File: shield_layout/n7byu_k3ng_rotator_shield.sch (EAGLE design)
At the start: 23 parts, among them J1 ARDUINO_R3_SHIELD

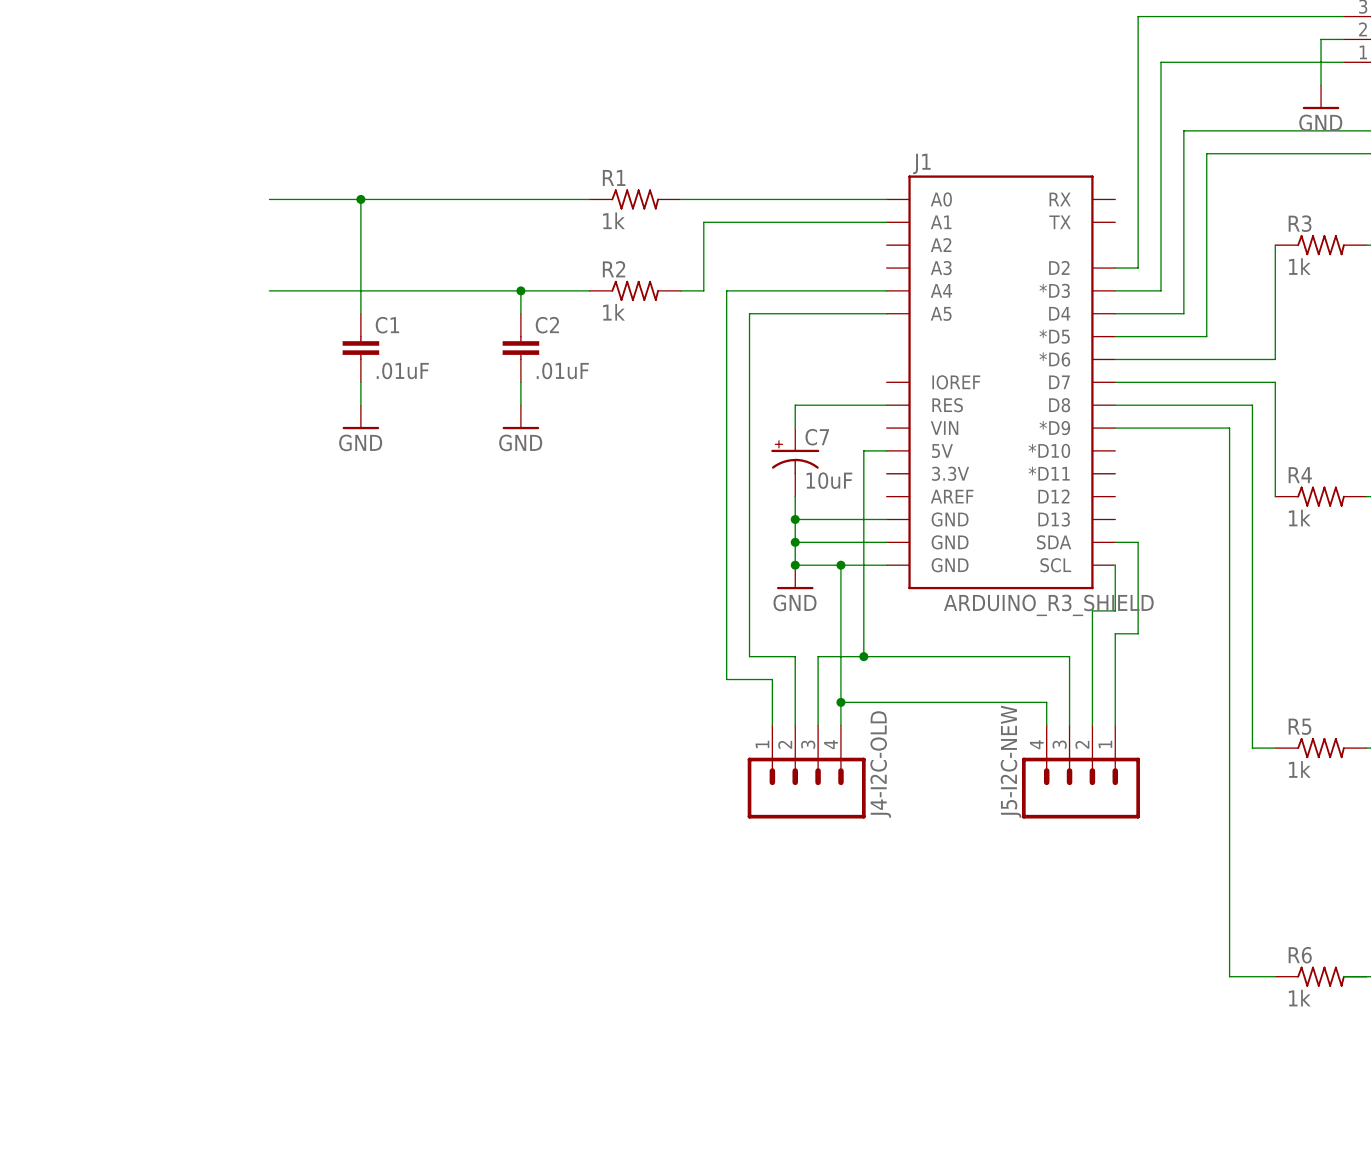
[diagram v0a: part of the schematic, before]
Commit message: jumpers for park, stop, reset buttons
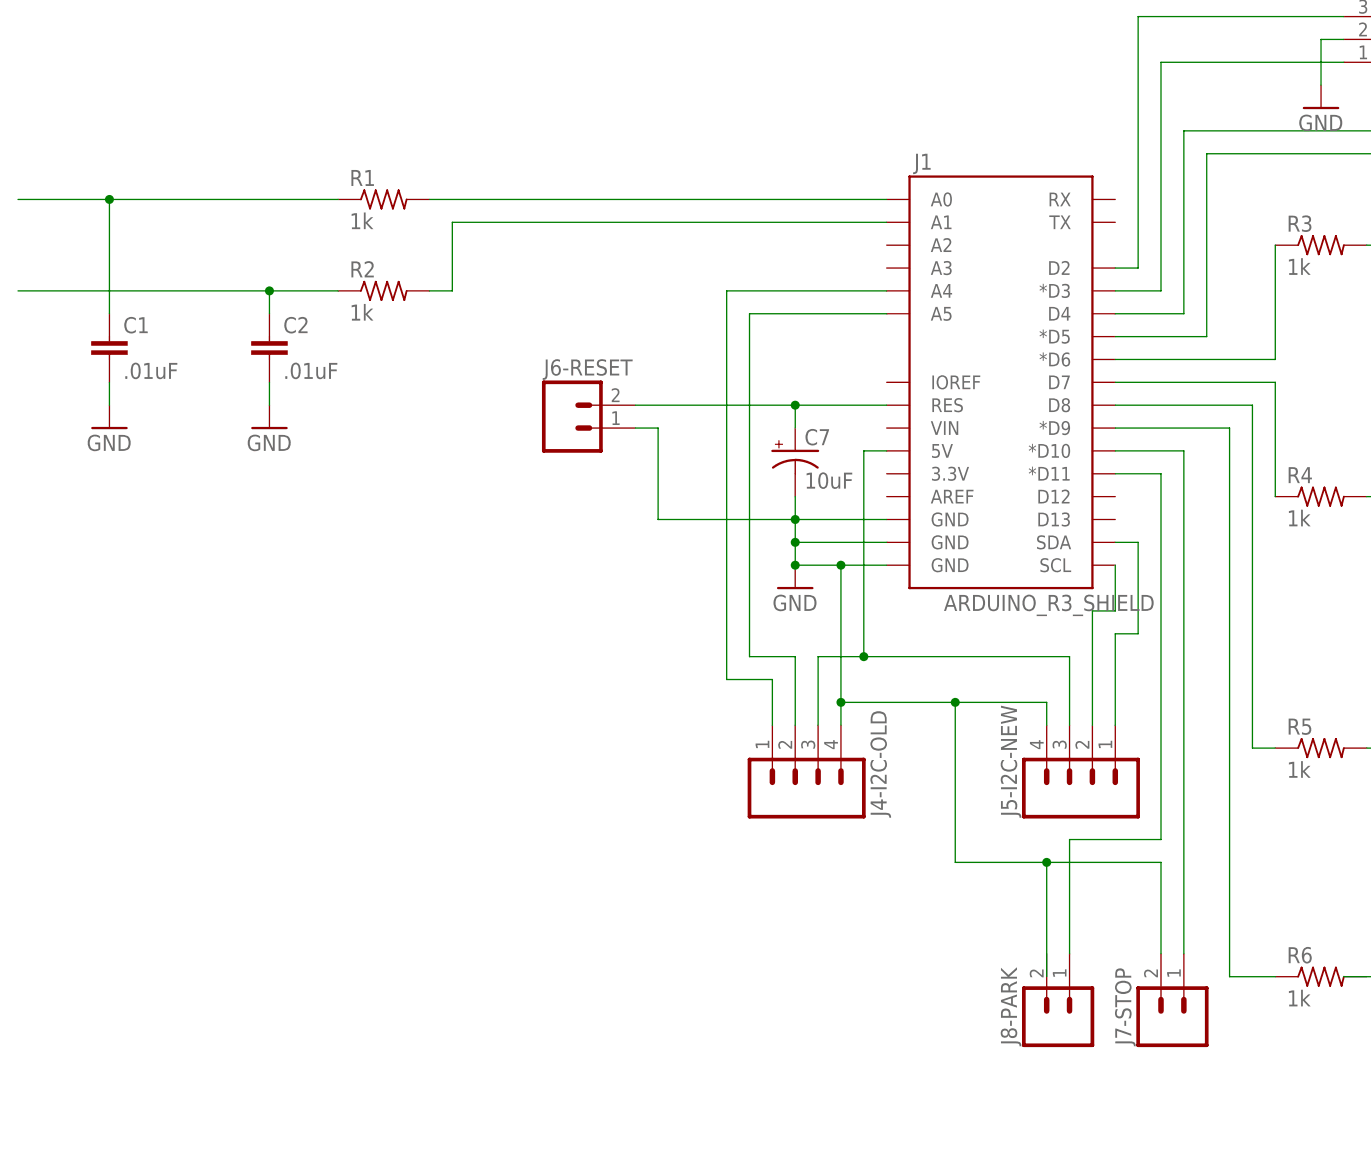
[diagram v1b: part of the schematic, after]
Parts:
- added J6-RESET, J7-STOP, J8-PARK: (no value), SparkFun-Connectors:M02PTH3
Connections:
- new net N$28: J1.*D10, J7-STOP.1
- new net N$29: J1.*D11, J8-PARK.1
- net GND: now also J6-RESET.1, J7-STOP.2
- net N$13: now also J6-RESET.2
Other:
- moved on the sheet: C1, C2, R1, R2
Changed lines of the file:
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@@
 <part name="J4-I2C-OLD" library="SparkFun-Connectors" deviceset="M04" device="LONGPADS"/>
 <part name="J5-I2C-NEW" library="SparkFun-Connectors" deviceset="M04" device="LONGPADS"/>
+<part name="J6-RESET" library="SparkFun-Connectors" deviceset="M02" device="PTH3"/>
+<part name="J7-STOP" library="SparkFun-Connectors" deviceset="M02" device="PTH3"/>
+<part name="J8-PARK" library="SparkFun-Connectors" deviceset="M02" device="PTH3"/>
 </parts>
 <sheets>
@@
 </plain>
 <instances>
-<instance part="R1" gate="G$1" x="68.58" y="71.12"/>
-<instance part="R2" gate="G$1" x="68.58" y="60.96"/>
+<instance part="R1" gate="G$1" x="40.64" y="71.12"/>
+<instance part="R2" gate="G$1" x="40.64" y="60.96"/>
 <instance part="R3" gate="G$1" x="144.78" y="66.04"/>
 <instance part="R4" gate="G$1" x="144.78" y="38.1"/>
 <instance part="R5" gate="G$1" x="144.78" y="10.16"/>
 <instance part="R6" gate="G$1" x="144.78" y="-15.24"/>
-<instance part="C1" gate="G$1" x="38.1" y="53.34"/>
-<instance part="C2" gate="G$1" x="55.88" y="53.34"/>
+<instance part="C1" gate="G$1" x="10.16" y="53.34"/>
+<instance part="C2" gate="G$1" x="27.94" y="53.34"/>
 <instance part="C3" gate="G$1" x="185.42" y="66.04"/>
 <instance part="C4" gate="G$1" x="185.42" y="38.1"/>
@@
 <instance part="Q4" gate="G$1" x="160.02" y="-15.24"/>
 <instance part="C7" gate="G$1" x="86.36" y="43.18"/>
-<instance part="GND1" gate="1" x="38.1" y="45.72"/>
-<instance part="GND2" gate="1" x="55.88" y="45.72"/>
+<instance part="GND1" gate="1" x="10.16" y="45.72"/>
+<instance part="GND2" gate="1" x="27.94" y="45.72"/>
 <instance part="GND3" gate="1" x="162.56" y="53.34"/>
 <instance part="GND4" gate="1" x="185.42" y="53.34"/>
@@
 <instance part="J4-I2C-OLD" gate="G$1" x="86.36" y="7.62" rot="MR90"/>
 <instance part="J5-I2C-NEW" gate="G$1" x="119.38" y="7.62" rot="R90"/>
+<instance part="J6-RESET" gate="G$1" x="60.96" y="45.72"/>
+<instance part="J7-STOP" gate="G$1" x="129.54" y="-20.32" rot="R90"/>
+<instance part="J8-PARK" gate="G$1" x="116.84" y="-20.32" rot="R90"/>
 </instances>
 <busses>
@@
 <segment>
 <pinref part="R1" gate="G$1" pin="2"/>
-<wire x1="73.66" y1="71.12" x2="96.52" y2="71.12" width="0.1524" layer="91"/>
+<wire x1="45.72" y1="71.12" x2="96.52" y2="71.12" width="0.1524" layer="91"/>
 <pinref part="J1" gate="G$1" pin="A0"/>
 </segment>
@@
 <pinref part="R1" gate="G$1" pin="1"/>
 <pinref part="C1" gate="G$1" pin="1"/>
-<wire x1="63.5" y1="71.12" x2="38.1" y2="71.12" width="0.1524" layer="91"/>
-<wire x1="38.1" y1="71.12" x2="38.1" y2="58.42" width="0.1524" layer="91"/>
-<junction x="38.1" y="71.12"/>
-<wire x1="38.1" y1="71.12" x2="27.94" y2="71.12" width="0.1524" layer="91"/>
+<wire x1="35.56" y1="71.12" x2="10.16" y2="71.12" width="0.1524" layer="91"/>
+<wire x1="10.16" y1="71.12" x2="10.16" y2="58.42" width="0.1524" layer="91"/>
+<junction x="10.16" y="71.12"/>
+<wire x1="10.16" y1="71.12" x2="0" y2="71.12" width="0.1524" layer="91"/>
 </segment>
 </net>
@@
 <pinref part="R2" gate="G$1" pin="1"/>
 <pinref part="C2" gate="G$1" pin="1"/>
-<wire x1="63.5" y1="60.96" x2="55.88" y2="60.96" width="0.1524" layer="91"/>
-<wire x1="55.88" y1="60.96" x2="55.88" y2="58.42" width="0.1524" layer="91"/>
-<junction x="55.88" y="60.96"/>
-<wire x1="55.88" y1="60.96" x2="27.94" y2="60.96" width="0.1524" layer="91"/>
+<wire x1="35.56" y1="60.96" x2="27.94" y2="60.96" width="0.1524" layer="91"/>
+<wire x1="27.94" y1="60.96" x2="27.94" y2="58.42" width="0.1524" layer="91"/>
+<junction x="27.94" y="60.96"/>
+<wire x1="27.94" y1="60.96" x2="0" y2="60.96" width="0.1524" layer="91"/>
 </segment>
 </net>
@@
 <segment>
 <pinref part="R2" gate="G$1" pin="2"/>
-<wire x1="73.66" y1="60.96" x2="76.2" y2="60.96" width="0.1524" layer="91"/>
-<wire x1="76.2" y1="60.96" x2="76.2" y2="68.58" width="0.1524" layer="91"/>
-<wire x1="76.2" y1="68.58" x2="96.52" y2="68.58" width="0.1524" layer="91"/>
+<wire x1="45.72" y1="60.96" x2="48.26" y2="60.96" width="0.1524" layer="91"/>
+<wire x1="48.26" y1="60.96" x2="48.26" y2="68.58" width="0.1524" layer="91"/>
+<wire x1="48.26" y1="68.58" x2="96.52" y2="68.58" width="0.1524" layer="91"/>
 <pinref part="J1" gate="G$1" pin="A1"/>
 </segment>
@@
 <segment>
 <pinref part="C1" gate="G$1" pin="2"/>
-<wire x1="38.1" y1="50.8" x2="38.1" y2="48.26" width="0.1524" layer="91"/>
+<wire x1="10.16" y1="50.8" x2="10.16" y2="48.26" width="0.1524" layer="91"/>
 <pinref part="GND1" gate="1" pin="GND"/>
 </segment>
 <segment>
 <pinref part="C2" gate="G$1" pin="2"/>
-<wire x1="55.88" y1="50.8" x2="55.88" y2="48.26" width="0.1524" layer="91"/>
+<wire x1="27.94" y1="50.8" x2="27.94" y2="48.26" width="0.1524" layer="91"/>
 <pinref part="GND2" gate="1" pin="GND"/>
 </segment>
@@
 <junction x="86.36" y="30.48"/>
 <pinref part="J4-I2C-OLD" gate="G$1" pin="4"/>
-<wire x1="114.3" y1="15.24" x2="91.44" y2="15.24" width="0.1524" layer="91"/>
+<wire x1="114.3" y1="15.24" x2="104.14" y2="15.24" width="0.1524" layer="91"/>
+<wire x1="104.14" y1="15.24" x2="91.44" y2="15.24" width="0.1524" layer="91"/>
 <wire x1="91.44" y1="15.24" x2="91.44" y2="12.7" width="0.1524" layer="91"/>
 <wire x1="91.44" y1="15.24" x2="91.44" y2="30.48" width="0.1524" layer="91"/>
@@
 <pinref part="J5-I2C-NEW" gate="G$1" pin="4"/>
 <wire x1="114.3" y1="15.24" x2="114.3" y2="12.7" width="0.1524" layer="91"/>
+<pinref part="J7-STOP" gate="G$1" pin="2"/>
+<wire x1="127" y1="-12.7" x2="127" y2="-2.54" width="0.1524" layer="91"/>
+<wire x1="127" y1="-2.54" x2="114.3" y2="-2.54" width="0.1524" layer="91"/>
+<wire x1="114.3" y1="-15.24" x2="114.3" y2="-2.54" width="0.1524" layer="91"/>
+<wire x1="114.3" y1="-2.54" x2="104.14" y2="-2.54" width="0.1524" layer="91"/>
+<junction x="114.3" y="-2.54"/>
+<wire x1="104.14" y1="-2.54" x2="104.14" y2="15.24" width="0.1524" layer="91"/>
+<junction x="104.14" y="15.24"/>
+<pinref part="J6-RESET" gate="G$1" pin="1"/>
+<wire x1="68.58" y1="45.72" x2="71.12" y2="45.72" width="0.1524" layer="91"/>
+<wire x1="71.12" y1="45.72" x2="71.12" y2="35.56" width="0.1524" layer="91"/>
+<wire x1="71.12" y1="35.56" x2="86.36" y2="35.56" width="0.1524" layer="91"/>
 </segment>
 <segment>
@@
 <pinref part="C7" gate="G$1" pin="+"/>
 <wire x1="86.36" y1="48.26" x2="86.36" y2="45.72" width="0.1524" layer="91"/>
+<pinref part="J6-RESET" gate="G$1" pin="2"/>
+<wire x1="86.36" y1="48.26" x2="68.58" y2="48.26" width="0.1524" layer="91"/>
+<junction x="86.36" y="48.26"/>
 </segment>
 </net>
@@
 </segment>
 </net>
+<net name="N$28" class="0">
+<segment>
+<pinref part="J1" gate="G$1" pin="*D10"/>
+<wire x1="121.92" y1="43.18" x2="129.54" y2="43.18" width="0.1524" layer="91"/>
+<pinref part="J7-STOP" gate="G$1" pin="1"/>
+<wire x1="129.54" y1="43.18" x2="129.54" y2="-12.7" width="0.1524" layer="91"/>
+</segment>
+</net>
+<net name="N$29" class="0">
+<segment>
+<pinref part="J1" gate="G$1" pin="*D11"/>
+<wire x1="121.92" y1="40.64" x2="127" y2="40.64" width="0.1524" layer="91"/>
+<wire x1="127" y1="40.64" x2="127" y2="0" width="0.1524" layer="91"/>
+<wire x1="127" y1="0" x2="116.84" y2="0" width="0.1524" layer="91"/>
+<pinref part="J8-PARK" gate="G$1" pin="1"/>
+<wire x1="116.84" y1="0" x2="116.84" y2="-12.7" width="0.1524" layer="91"/>
+</segment>
+</net>
